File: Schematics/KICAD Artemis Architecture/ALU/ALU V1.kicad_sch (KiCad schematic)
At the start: 11 parts, among them J1 B Input, J2 A Input, J3 Bus, J4 Control, J5 Flags, J6 Power, U1 74LS181, U2 74LS181, U3 74LS30, U4 74LS245

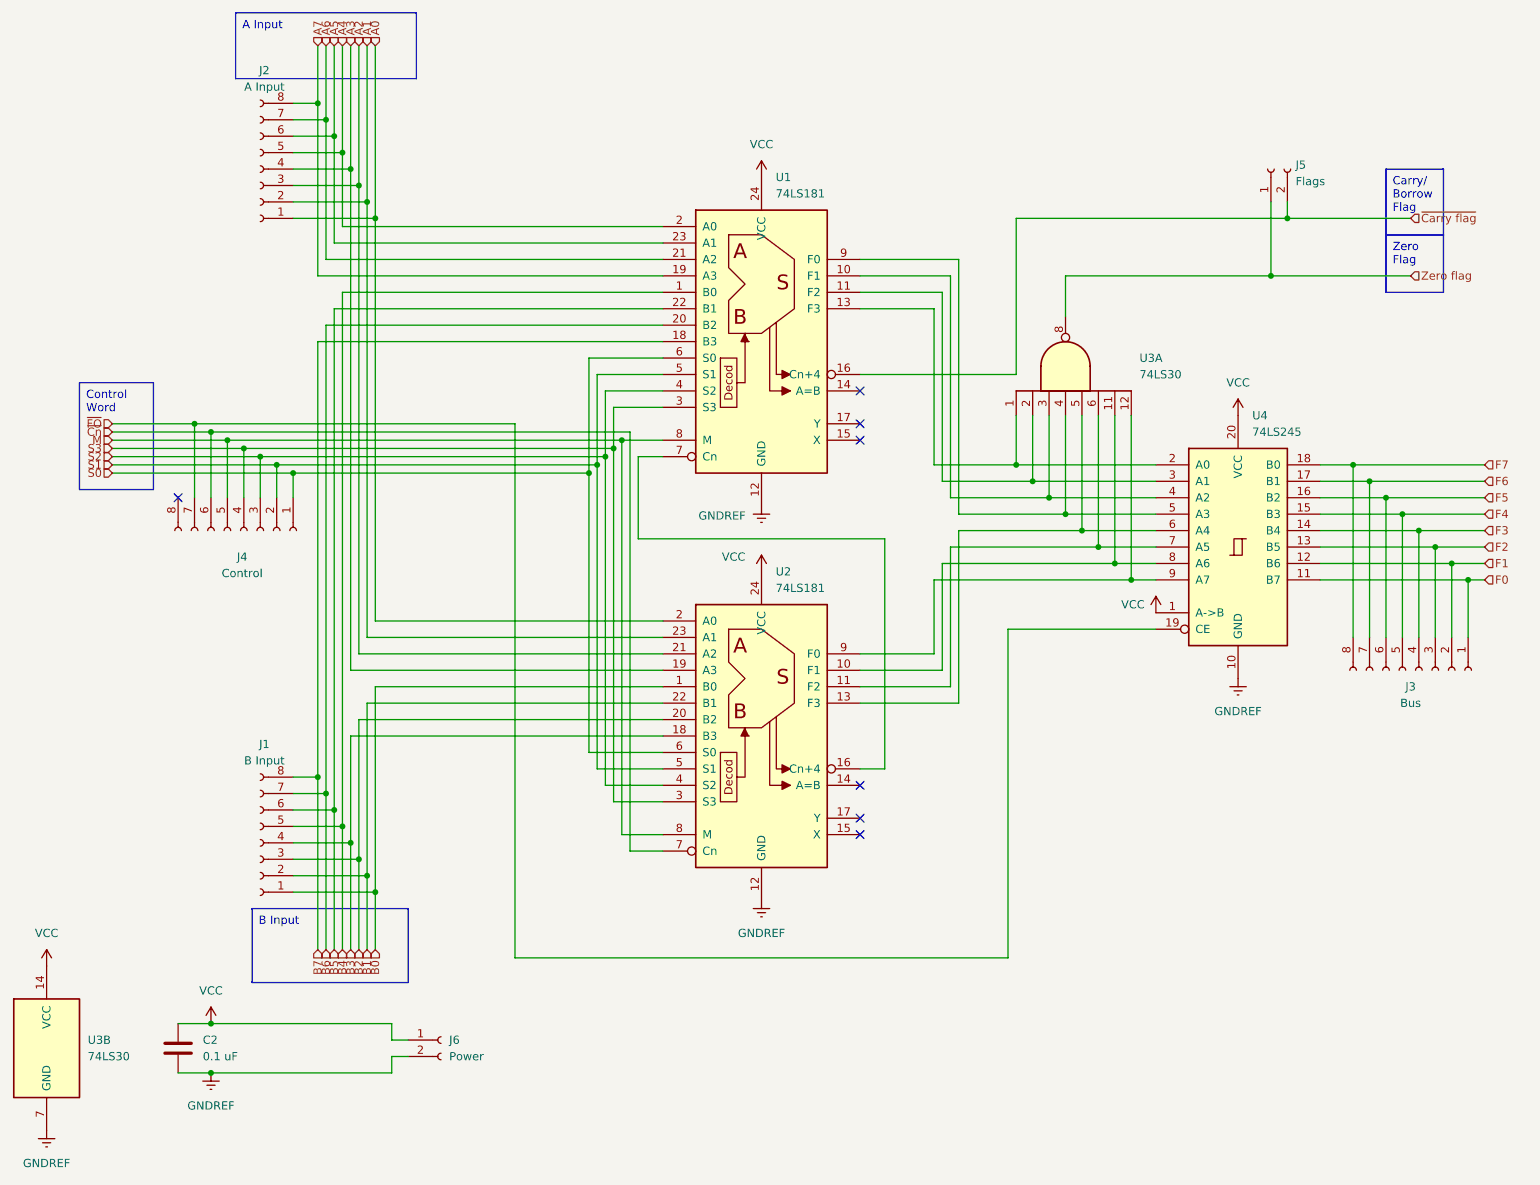
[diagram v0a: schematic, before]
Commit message: ALU PCB and Schematic Redesign
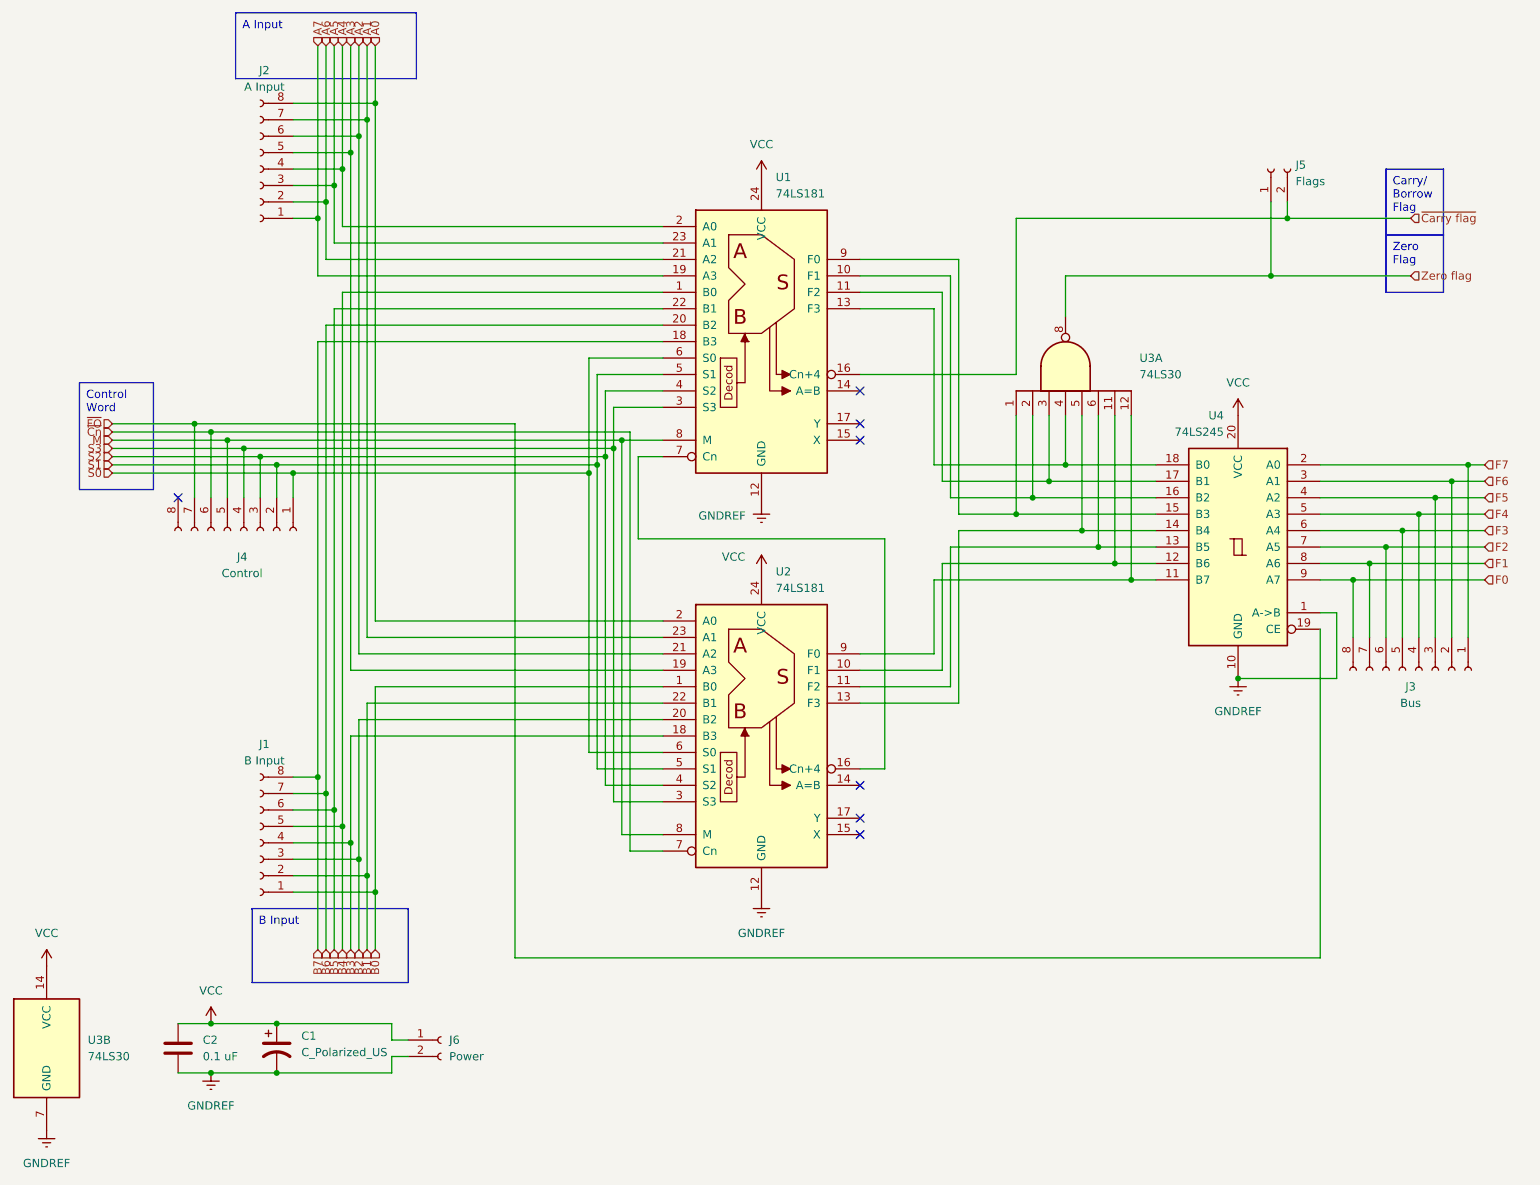
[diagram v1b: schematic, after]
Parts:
- added C1: C_Polarized_US, Capacitor_THT:CP_Radial_D6.3mm_P2.50mm, symbol Device:C_Polarized_US
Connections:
- net A0: now also J2.8 (Pin_8); no longer J2.1 (Pin_1)
- net A1: now also J2.7 (Pin_7); no longer J2.2 (Pin_2)
- net A2: now also J2.6 (Pin_6); no longer J2.3 (Pin_3)
- net A3: now also J2.5 (Pin_5); no longer J2.4 (Pin_4)
- net A4: now also J2.4 (Pin_4); no longer J2.5 (Pin_5)
- net A5: now also J2.3 (Pin_3); no longer J2.6 (Pin_6)
- net A6: now also J2.2 (Pin_2); no longer J2.7 (Pin_7)
- net A7: now also J2.1 (Pin_1); no longer J2.8 (Pin_8)
- net F0: now also J3.8 (Pin_8), U4.9 (A7); no longer J3.1 (Pin_1), U4.11 (B7)
- net F1: now also J3.7 (Pin_7), U4.8 (A6); no longer J3.2 (Pin_2), U4.12 (B6)
- net F2: now also J3.6 (Pin_6), U4.7 (A5); no longer J3.3 (Pin_3), U4.13 (B5)
- net F3: now also J3.5 (Pin_5), U4.6 (A4); no longer J3.4 (Pin_4), U4.14 (B4)
- net F4: now also J3.4 (Pin_4), U4.5 (A3); no longer J3.5 (Pin_5), U4.15 (B3)
- net F5: now also J3.3 (Pin_3), U4.4 (A2); no longer J3.6 (Pin_6), U4.16 (B2)
- net F6: now also J3.2 (Pin_2), U4.3 (A1); no longer J3.7 (Pin_7), U4.17 (B1)
- net F7: now also J3.1 (Pin_1), U4.2 (A0); no longer J3.8 (Pin_8), U4.18 (B0)
- net GNDREF: now also U4.1 (A->B), C1.2
- net VCC: now also C1.1; no longer U4.1 (A->B)
- net at U2.13 (F3), U3.5: now also U4.14 (B4); no longer U4.6 (A4)
- net at U2.11 (F2), U3.6: now also U4.13 (B5); no longer U4.7 (A5)
- net at U2.10 (F1), U3.11: now also U4.12 (B6); no longer U4.8 (A6)
- net at U2.9 (F0), U3.12: now also U4.11 (B7); no longer U4.9 (A7)
- new net: U1.9 (F0), U3.1, U4.15 (B3)
- new net: U1.10 (F1), U3.2, U4.16 (B2)
- new net: U1.11 (F2), U3.3, U4.17 (B1)
- new net: U1.13 (F3), U3.4, U4.18 (B0)
